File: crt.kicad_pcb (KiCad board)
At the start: 2 copper layers, 103 x 80 mm, 127 parts, among them J1 Video, J2 H_COIL, J3 V_COIL, J4 CRT, J5 Barrel_Jack, Q1 BC847, Q2 2N5551, Q3 9013, Q4 9013, Q5 NPN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

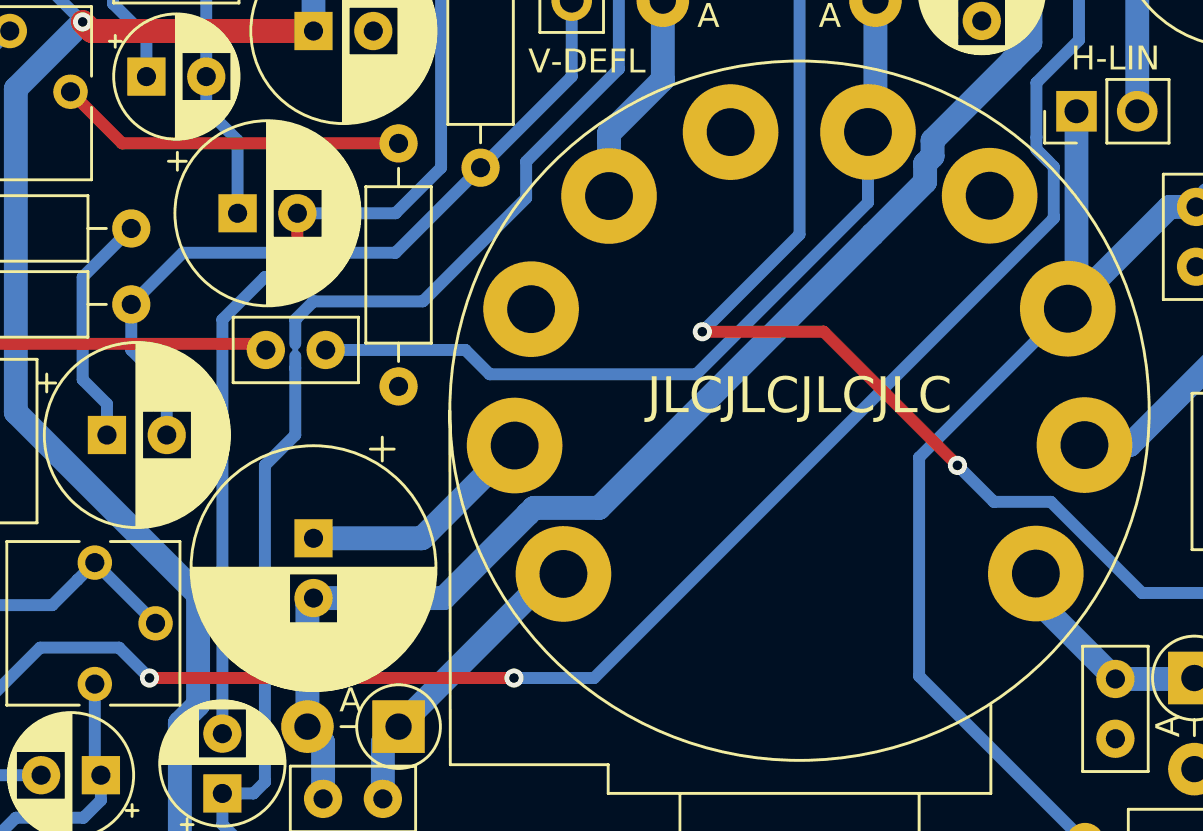
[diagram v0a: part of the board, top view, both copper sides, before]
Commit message: fix munting pads, camera ready?
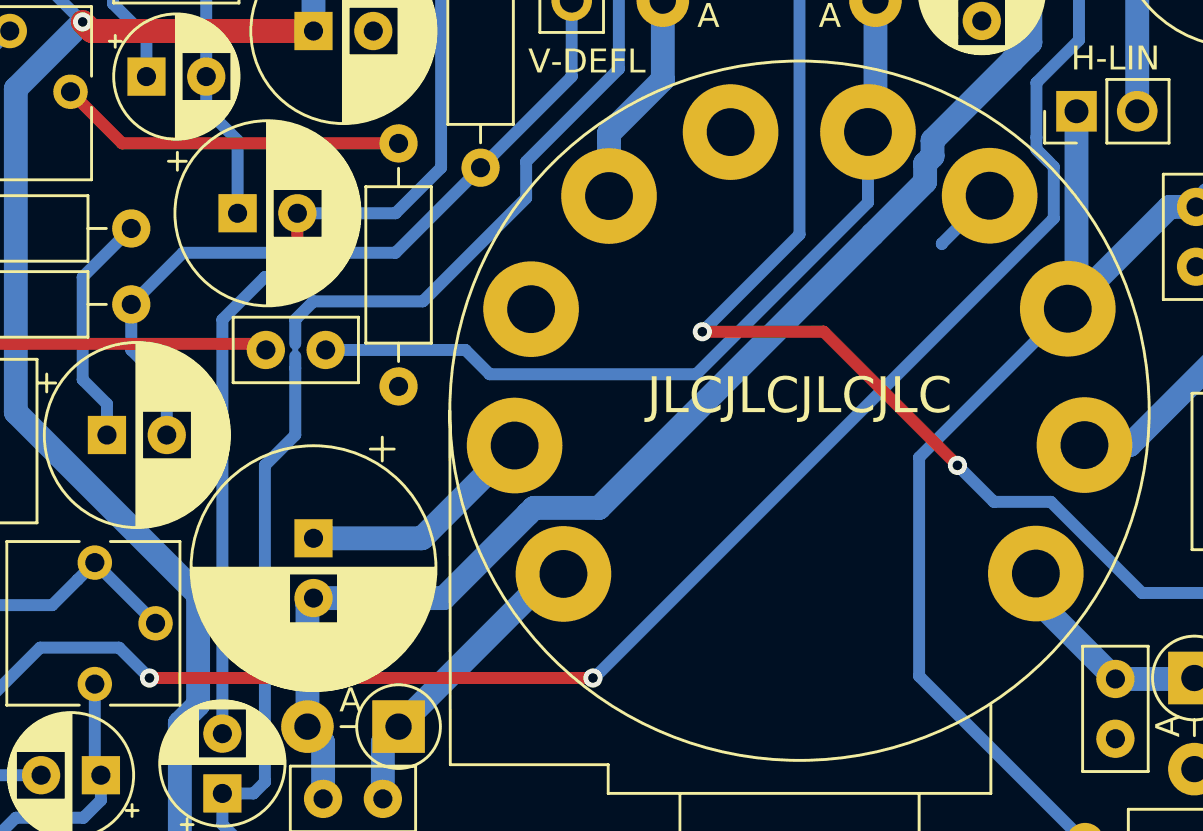
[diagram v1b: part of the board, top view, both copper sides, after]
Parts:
- removed the REF** at (211.0, 125.0)
- removed the REF** at (211.0, 56.0)
- removed the REF** at (118.0, 56.0)
- removed the REF** at (133.0, 119.0)
- added H1: MountingHole_Pad, MountingHole:MountingHole_3.2mm_M3_Pad_Via, F.Cu at (118.0, 56.0)
- added H2: MountingHole_Pad, MountingHole:MountingHole_3.2mm_M3_Pad_Via, F.Cu at (133.0, 119.0)
- added H3: MountingHole_Pad, MountingHole:MountingHole_3.2mm_M3_Pad_Via, F.Cu at (211.0, 56.0)
- added H4: MountingHole_Pad, MountingHole:MountingHole_3.2mm_M3_Pad_Via, F.Cu at (211.0, 125.0)
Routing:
- net GND: track 0.00 -> 2.85 mm
